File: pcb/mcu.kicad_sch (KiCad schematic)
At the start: 4 parts, among them J1 Conn_01x04, SW1 TS-1088-AR02016, U1 STC8H1K08-TSSOP20

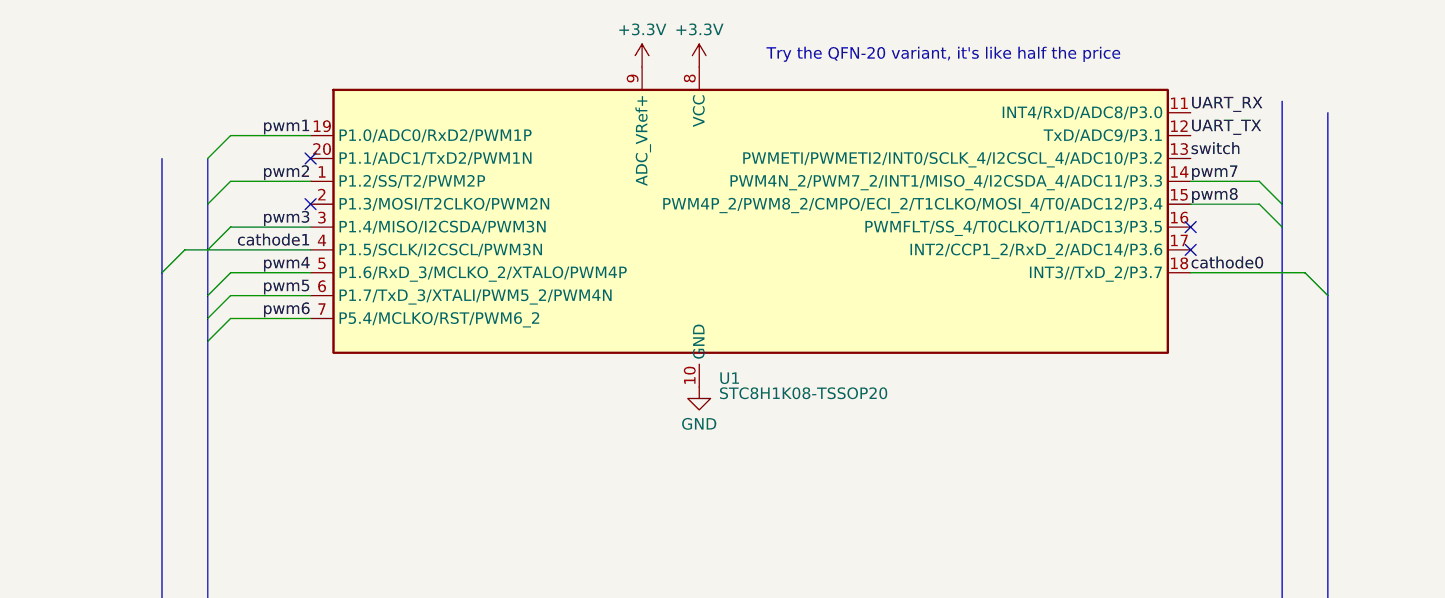
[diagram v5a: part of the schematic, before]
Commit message: Try swapping to a qfn part instead of tssop-20
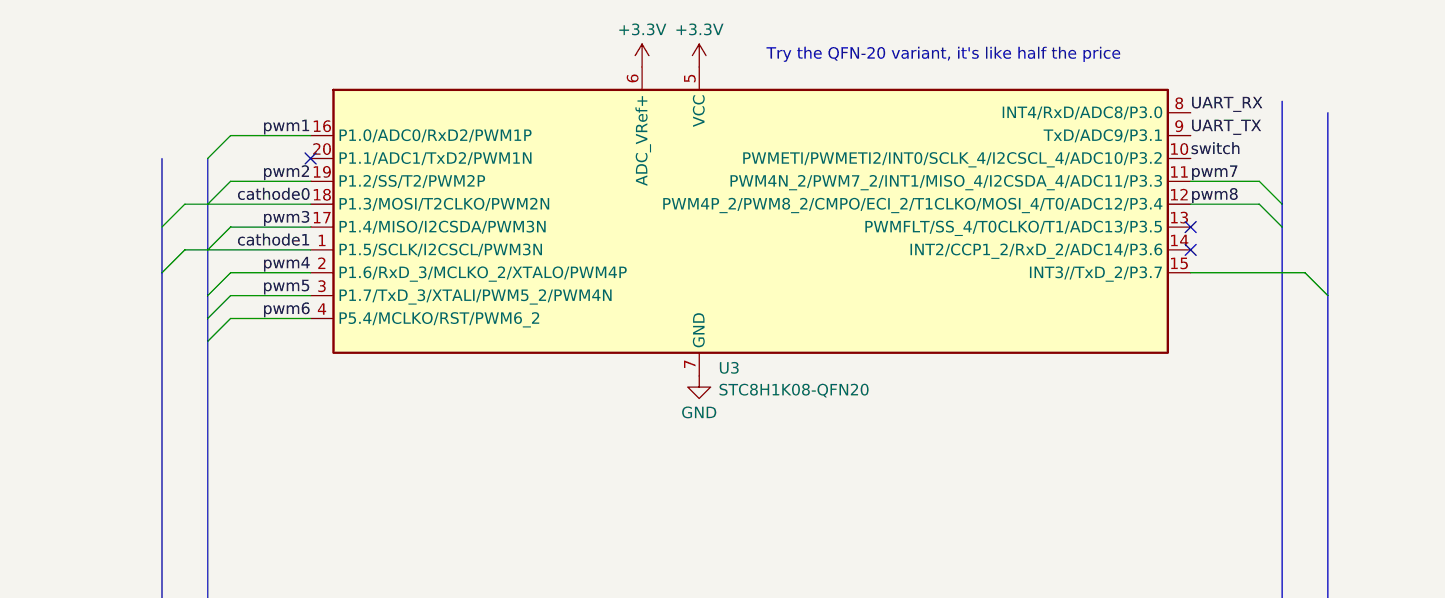
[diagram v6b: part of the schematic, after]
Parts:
- removed U1: STC8H1K08-TSSOP20, Package_SO:TSSOP-20_4.4x6.5mm_P0.65mm, symbol stc8h:STC8H1K08
- added U3: STC8H1K08-QFN20, Package_DFN_QFN:QFN-20-1EP_3x3mm_P0.4mm_EP1.65x1.65mm, symbol stc8h:STC8H1K08-QFN20
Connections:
- net +3.3V: now also U3.5 (VCC), U3.6 (ADC_VRef+)
- net UART_RX: now also U3.8 (INT4/RxD/ADC8/P3.0)
- net UART_TX: now also U3.9 (TxD/ADC9/P3.1)
- net cathode0: now also U3.18 (P1.3/MOSI/T2CLKO/PWM2N)
- net cathode1: now also U3.1 (P1.5/SCLK/I2CSCL/PWM3N)
- net pwm1: now also U3.16 (P1.0/ADC0/RxD2/PWM1P)
- net pwm2: now also U3.19 (P1.2/SS/T2/PWM2P)
- net pwm3: now also U3.17 (P1.4/MISO/I2CSDA/PWM3N)
- net pwm4: now also U3.2 (P1.6/RxD_3/MCLKO_2/XTALO/PWM4P)
- net pwm5: now also U3.3 (P1.7/TxD_3/XTALI/PWM5_2/PWM4N)
- net pwm6: now also U3.4 (P5.4/MCLKO/RST/PWM6_2)
- net pwm7: now also U3.11 (PWM4N_2/PWM7_2/INT1/MISO_4/I2CSDA_4/ADC11/P3.3)
- net pwm8: now also U3.12 (PWM4P_2/PWM8_2/CMPO/ECI_2/T1CLKO/MOSI_4/T0/ADC12/P3.4)
- net switch: now also U3.10 (PWMETI/PWMETI2/INT0/SCLK_4/I2CSCL_4/ADC10/P3.2)
- net GND renamed EP
- net EP: now also U3.21 (EP), U3.7 (GND)
- no-connect marks 4 -> 3
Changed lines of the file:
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@@
-	)
-	(no_connect
-		(at 97.79 35.56)
 	)
 	(no_connect
@@
 	)
 	(bus_entry
+		(at 81.28 38.1)
+		(size 2.54 -2.54)
+		(stroke
+			(width 0)
+			(type default)
+		)
+	)
+	(bus_entry
 		(at 86.36 48.26)
 		(size 2.54 -2.54)
@@
 		)
 	)
+	(wire
+		(pts
+			(xy 86.36 35.56) (xy 97.79 35.56)
+		)
+		(stroke
+			(width 0)
+			(type default)
+		)
+	)
 	(bus
 		(pts
@@
 		(pts
 			(xy 88.9 48.26) (xy 97.79 48.26)
+		)
+		(stroke
+			(width 0)
+			(type default)
+		)
+	)
+	(wire
+		(pts
+			(xy 83.82 35.56) (xy 86.36 35.56)
 		)
 		(stroke
@@
 	)
 	(label "cathode0"
-		(at 195.58 43.18 0)
-		(effects
-			(font
-				(size 1.27 1.27)
-			)
-			(justify left bottom)
+		(at 97.79 35.56 180)
+		(effects
+			(font
+				(size 1.27 1.27)
+			)
+			(justify right bottom)
 		)
 	)
@@
 			)
 			(justify left)
+		)
+	)
+	(symbol
+		(lib_id "stc8h:STC8H1K08-QFN20")
+		(at 140.97 38.1 0)
+		(unit 1)
+		(body_style 1)
+		(exclude_from_sim no)
+		(in_bom yes)
+		(on_board yes)
+		(in_pos_files yes)
+		(dnp no)
+		(fields_autoplaced yes)
+		(property "Reference" "U3"
+			(at 143.1133 53.7901 0)
+			(show_name no)
+			(do_not_autoplace no)
+			(effects
+				(font
+					(size 1.27 1.27)
+				)
+				(justify left)
+			)
+		)
+		(property "Value" "STC8H1K08-QFN20"
+			(at 143.1133 56.2144 0)
+			(show_name no)
+			(do_not_autoplace no)
+			(effects
+				(font
+					(size 1.27 1.27)
+				)
+				(justify left)
+			)
+		)
+		(property "Footprint" "Package_DFN_QFN:QFN-20-1EP_3x3mm_P0.4mm_EP1.65x1.65mm"
+			(at 140.97 38.1 0)
+			(hide yes)
+			(show_name no)
+			(do_not_autoplace no)
+			(effects
+				(font
+					(size 1.27 1.27)
+				)
+			)
+		)
+		(property "Datasheet" ""
+			(at 140.97 38.1 0)
+			(hide yes)
+			(show_name no)
+			(do_not_autoplace no)
+			(effects
+				(font
+					(size 1.27 1.27)
+				)
+			)
+		)
+		(property "Description" ""
+			(at 140.97 38.1 0)
+			(hide yes)
+			(show_name no)
+			(do_not_autoplace no)
+			(effects
+				(font
+					(size 1.27 1.27)
+				)
+			)
+		)
+		(property "LCSC" "C915674"
+			(at 140.97 38.1 0)
+			(hide yes)
+			(show_name no)
+			(do_not_autoplace no)
+			(effects
+				(font
+					(size 1.27 1.27)
+				)
+			)
+		)
+		(pin "3"
+		)
+		(pin "10"
+		)
+		(pin "8"
+		)
+		(pin "17"
+		)
+		(pin "12"
+		)
+		(pin "9"
+		)
+		(pin "4"
+		)
+		(pin "15"
+		)
+		(pin "11"
+		)
+		(pin "1"
+		)
+		(pin "2"
+		)
+		(pin "13"
+		)
+		(pin "6"
+		)
+		(pin "19"
+		)
+		(pin "7"
+		)
+		(pin "16"
+		)
+		(pin "5"
+		)
+		(pin "14"
+		)
+		(pin "20"
+		)
+		(pin "21"
+		)
+		(pin "18"
+		)
+		(instances
+			(project "nametag"
+				(path "/a7c50b29-e914-4aee-9ec8-81f37f7bd068/858a59c4-d6e3-4a1e-955d-510d1161f2bb"
+					(reference "U3")
+					(unit 1)
+				)
+			)
 		)
 	)
@@
 	(symbol
 		(lib_id "power:GND")
-		(at 140.97 55.88 0)
+		(at 140.97 54.61 0)
 		(unit 1)
 		(body_style 1)
@@
 		(fields_autoplaced yes)
 		(property "Reference" "#PWR018"
-			(at 140.97 62.23 0)
+			(at 140.97 60.96 0)
 			(hide yes)
 			(show_name no)
@@
 		)
 		(property "Value" "GND"
-			(at 140.97 60.0131 0)
+			(at 140.97 58.7431 0)
 			(show_name no)
 			(do_not_autoplace no)
@@
 		)
 		(property "Footprint" ""
-			(at 140.97 55.88 0)
+			(at 140.97 54.61 0)
 			(hide yes)
 			(show_name no)
@@
 		)
 		(property "Datasheet" ""
-			(at 140.97 55.88 0)
+			(at 140.97 54.61 0)
 			(hide yes)
 			(show_name no)
@@
 		)
 		(property "Description" "Power symbol creates a global label with name \"GND\" , ground"
-			(at 140.97 55.88 0)
+			(at 140.97 54.61 0)
 			(hide yes)
 			(show_name no)
@@
 					(unit 1)
 				)
-			)
-		)
-	)
-	(symbol
-		(lib_id "stc8h:STC8H1K08")
-		(at 140.97 38.1 0)
-		(unit 1)
-		(body_style 1)
-		(exclude_from_sim no)
-		(in_bom yes)
-		(on_board yes)
-		(in_pos_files yes)
-		(dnp no)
-		(fields_autoplaced yes)
-		(property "Reference" "U1"
-			(at 143.1641 54.9331 0)
-			(show_name no)
-			(do_not_autoplace no)
-			(effects
-				(font
-					(size 1.27 1.27)
-				)
-				(justify left)
-			)
-		)
-		(property "Value" "STC8H1K08-TSSOP20"
-			(at 143.1641 56.6145 0)
-			(show_name no)
-			(do_not_autoplace no)
-			(effects
-				(font
-					(size 1.27 1.27)
-				)
-				(justify left)
-			)
-		)
-		(property "Footprint" "Package_SO:TSSOP-20_4.4x6.5mm_P0.65mm"
-			(at 140.97 38.1 0)
-			(hide yes)
-			(show_name no)
-			(do_not_autoplace no)
-			(effects
-				(font
-					(size 1.27 1.27)
-				)
-			)
-		)
-		(property "Datasheet" ""
-			(at 140.97 38.1 0)
-			(hide yes)
-			(show_name no)
-			(do_not_autoplace no)
-			(effects
-				(font
-					(size 1.27 1.27)
-				)
-			)
-		)
-		(property "Description" ""
-			(at 140.97 38.1 0)
-			(hide yes)
-			(show_name no)
-			(do_not_autoplace no)
-			(effects
-				(font
-					(size 1.27 1.27)
-				)
-			)
-		)
-		(property "LCSC" " C915673"
-			(at 140.97 38.1 0)
-			(hide yes)
-			(show_name no)
-			(do_not_autoplace no)
-			(effects
-				(font
-					(size 1.27 1.27)
-				)
-			)
-		)
-		(pin "6"
-		)
-		(pin "11"
-		)
-		(pin "4"
-		)
-		(pin "12"
-		)
-		(pin "14"
-		)
-		(pin "18"
-		)
-		(pin "7"
-		)
-		(pin "13"
-		)
-		(pin "17"
-		)
-		(pin "3"
-		)
-		(pin "8"
-		)
-		(pin "16"
-		)
-		(pin "2"
-		)
-		(pin "5"
-		)
-		(pin "1"
-		)
-		(pin "19"
-		)
-		(pin "9"
-		)
-		(pin "10"
-		)
-		(pin "20"
-		)
-		(pin "15"
-		)
-		(instances
-			(project "nametag"
-				(path "/a7c50b29-e914-4aee-9ec8-81f37f7bd068/858a59c4-d6e3-4a1e-955d-510d1161f2bb"
-					(reference "U1")
-					(unit 1)
-				)

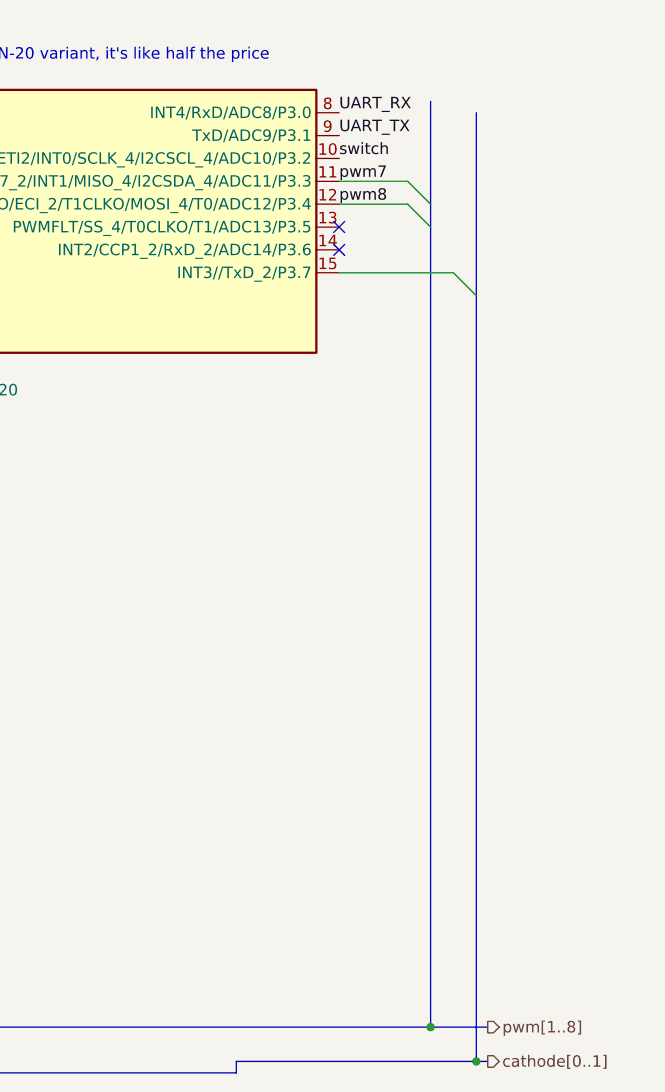
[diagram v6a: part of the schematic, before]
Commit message: Enlarge the PCB a bit
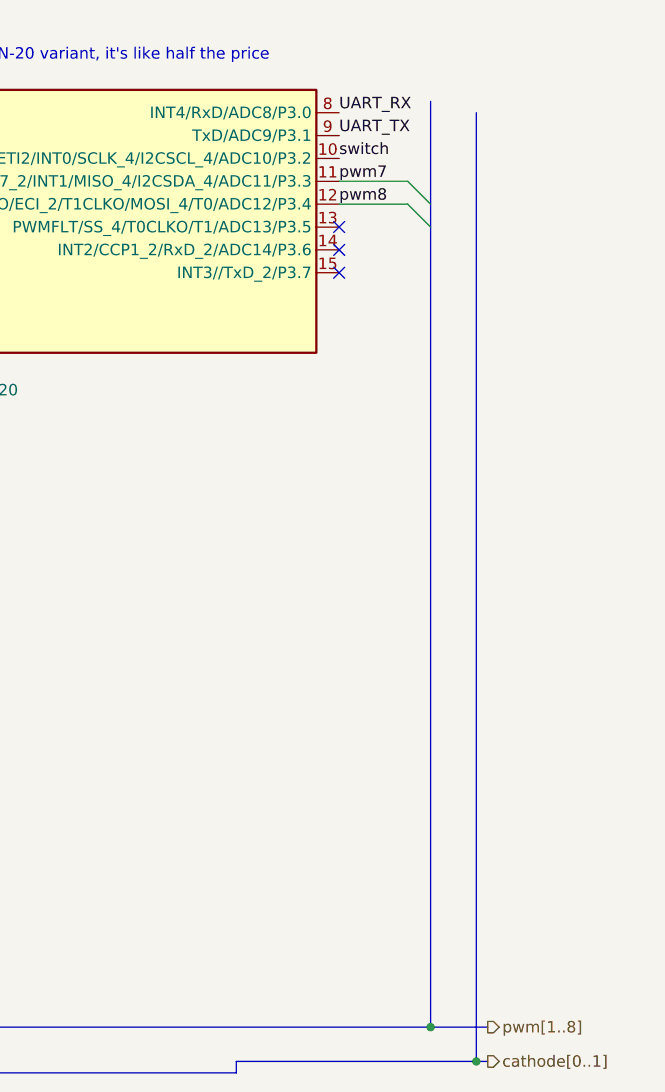
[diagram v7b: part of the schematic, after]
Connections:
- no-connect marks 3 -> 4
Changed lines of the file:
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@@
 		(at 97.79 30.48)
 	)
-	(bus_entry
-		(at 208.28 43.18)
-		(size 2.54 2.54)
-		(stroke
-			(width 0)
-			(type default)
-		)
+	(no_connect
+		(at 195.58 43.18)
 	)
 	(bus_entry
@@
 	(bus
 		(pts
-			(xy 210.82 45.72) (xy 210.82 130.81)
+			(xy 210.82 25.4) (xy 210.82 130.81)
 		)
 		(stroke
@@
 		)
 		(stroke
-			(width 0)
-			(type default)
-		)
-	)
-	(bus
-		(pts
-			(xy 210.82 25.4) (xy 210.82 45.72)
-		)
-		(stroke
-			(width 0)
-			(type default)
-		)
-	)
-	(wire
-		(pts
-			(xy 195.58 43.18) (xy 208.28 43.18)
-		)
-		(stroke

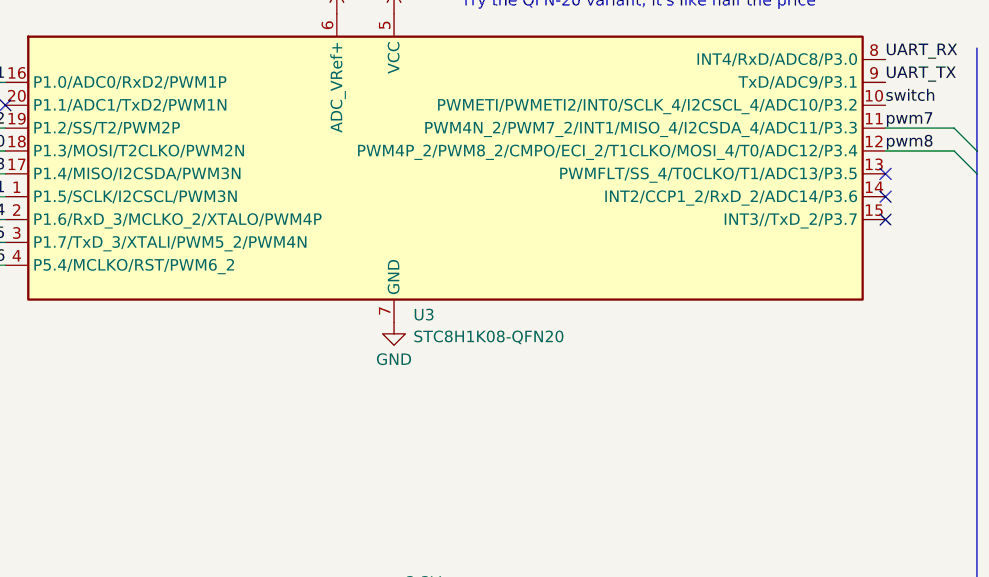
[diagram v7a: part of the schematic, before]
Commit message: Update footprints from LCSC EasyEDA Library
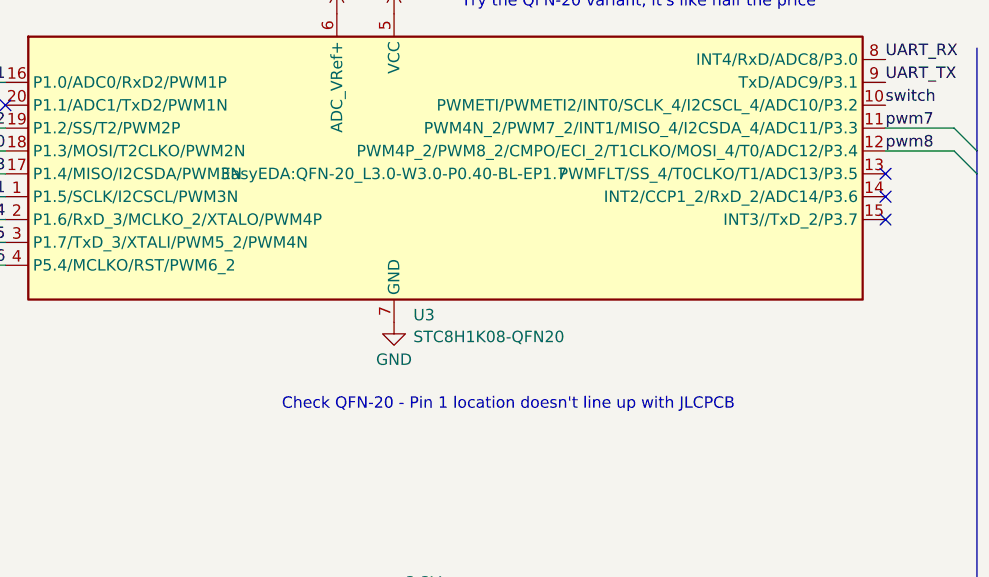
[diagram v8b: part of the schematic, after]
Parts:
- C2: footprint Capacitor_SMD:C_0603_1608Metric_Pad1.08x0.95mm_HandSolder -> Capacitor_SMD:C_0402_1005Metric
- SW1: footprint Button_Switch_SMD:SW_Push_SPST_NO_Alps_SKRK -> EasyEDA:SW-SMD_L3.9-W3.0-P4.45
- U3: footprint Package_DFN_QFN:QFN-20-1EP_3x3mm_P0.4mm_EP1.65x1.65mm -> EasyEDA:QFN-20_L3.0-W3.0-P0.40-BL-EP1.7
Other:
- note added: "Check QFN-20 - Pin 1 location doesn't line up with JLCPCB"
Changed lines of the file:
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@@
 	(generator_version "10.0")
 	(paper "A4")
+	(text "Check QFN-20 - Pin 1 location doesn't line up with JLCPCB"
+		(exclude_from_sim no)
+		(at 153.67 63.754 0)
+		(effects
+			(font
+				(size 1.27 1.27)
+			)
+		)
+	)
 	(text "Try the QFN-20 variant, it's like half the price"
 		(exclude_from_sim no)
@@
 			)
 		)
-		(property "Footprint" "Package_DFN_QFN:QFN-20-1EP_3x3mm_P0.4mm_EP1.65x1.65mm"
+		(property "Footprint" "EasyEDA:QFN-20_L3.0-W3.0-P0.40-BL-EP1.7"
 			(at 140.97 38.1 0)
-			(hide yes)
 			(show_name no)
 			(do_not_autoplace no)
@@
 			)
 		)
-		(property "Footprint" "Capacitor_SMD:C_0603_1608Metric_Pad1.08x0.95mm_HandSolder"
+		(property "Footprint" "Capacitor_SMD:C_0402_1005Metric"
 			(at 144.4752 95.25 0)
 			(hide yes)
@@
 			)
 		)
-		(property "Footprint" "Button_Switch_SMD:SW_Push_SPST_NO_Alps_SKRK"
+		(property "Footprint" "EasyEDA:SW-SMD_L3.9-W3.0-P4.45"
 			(at 38.1 106.68 0)
 			(hide yes)
